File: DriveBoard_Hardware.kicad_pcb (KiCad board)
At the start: 2 copper layers, 124.5 x 121.7 mm, 48 parts, among them SW1 SW_DPDT_x2, U1 MAX_3232, U10 Left Back, U11 TM4C129E_Launchpad_Full, U12 IRF7821PbF, U13 IRF7821PbF, U14 IRF7821PbF, U15 Strip_1, U16 Strip_2, U17 Servo_1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

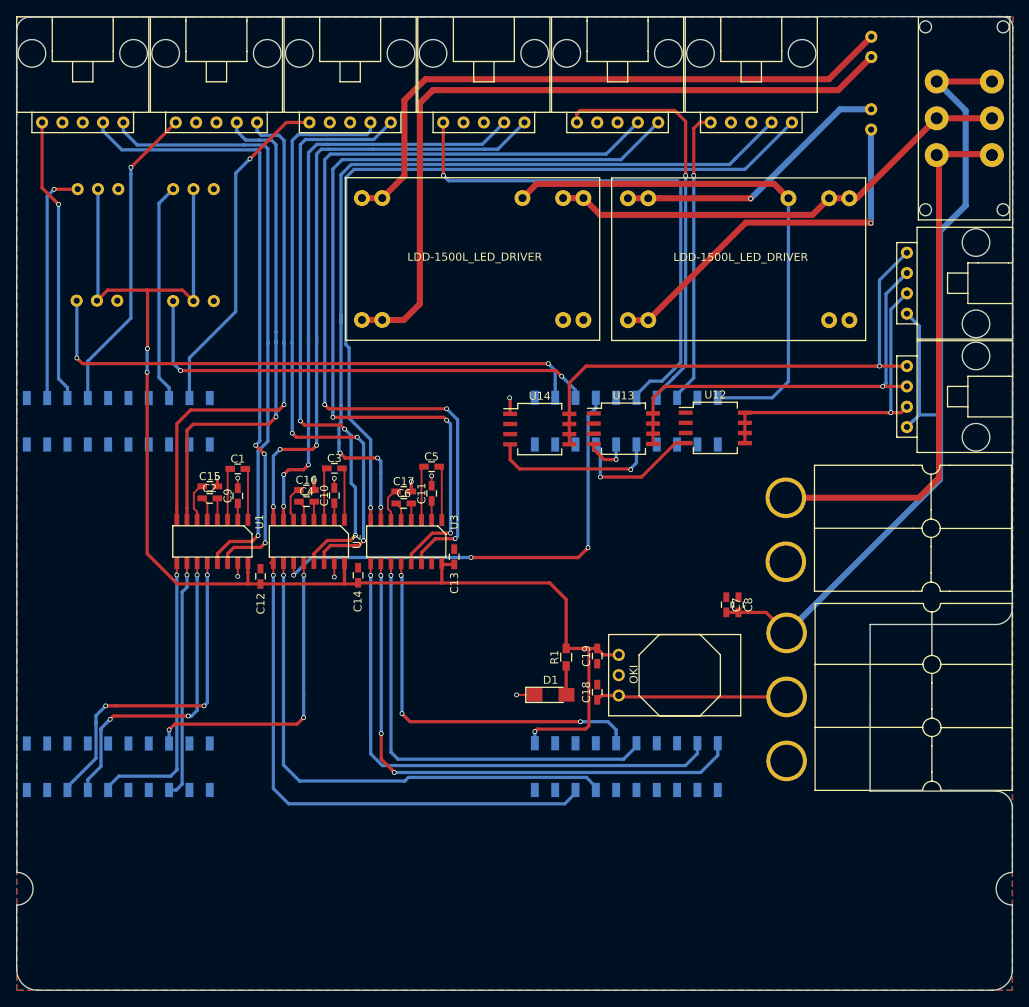
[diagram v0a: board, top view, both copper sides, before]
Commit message: Edited Schematic and added silkscreen
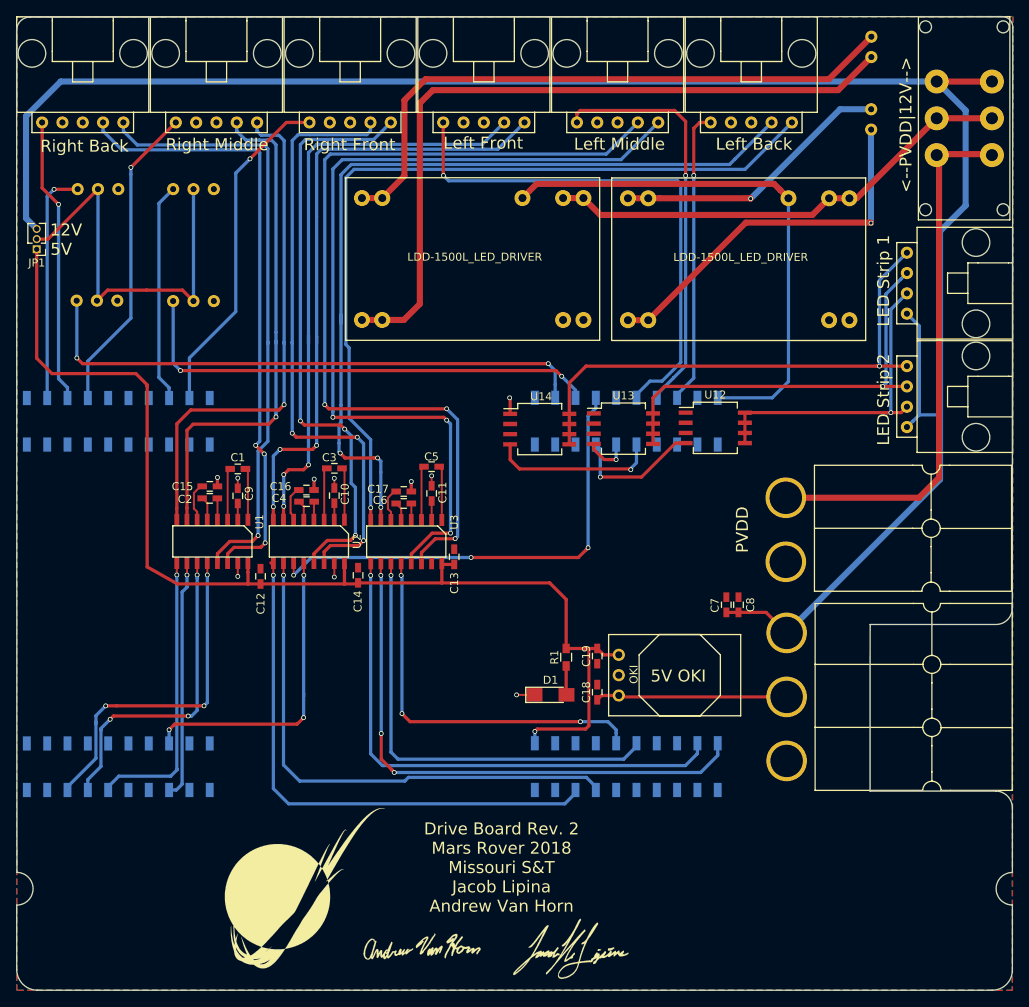
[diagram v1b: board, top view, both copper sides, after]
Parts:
- added G***: LOGO, MRDT_Silkscreens:MRDT_Logo_20mm, F.Cu at (169.7, 142.7)
- added G***: LOGO, MRDT_Silkscreens:Jacob_Lipina_Sig_15mm, F.Cu at (202.9, 150.5)
- added G***: LOGO, MRDT_Silkscreens:Andrew_Van_Horn_Sig_15mm, F.Cu at (184.3, 149.9)
- added JP1: Jumper_NC_Dual, Pin_Headers:Pin_Header_Straight_1x03_Pitch1.27mm, F.Cu at (136.2, 62.9)
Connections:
- U10 pad 2: (no net) -> Net-(U10-Pad2)
- U11 pad +5V: Net-(U11-Pad+5V) -> +5V
- U11 pad PB2: (no net) -> Net-(U11-PadPB2)
- U11 pad PB3: (no net) -> Net-(U11-PadPB3)
- U11 pad PD0: (no net) -> Net-(U11-PadPD0)
- U11 pad PD1: (no net) -> Net-(U11-PadPD1)
- U11 pad PD3: (no net) -> Net-(U11-PadPD3)
- U11 pad PD7: (no net) -> Net-(U11-PadPD7)
- U11 pad PE0: (no net) -> Net-(U11-PadPE0)
- U11 pad PE1: (no net) -> Net-(U11-PadPE1)
- U11 pad PE2: (no net) -> Net-(U11-PadPE2)
- U11 pad PE3: (no net) -> Net-(U11-PadPE3)
- U11 pad PE4: (no net) -> Net-(U11-PadPE4)
- U11 pad PE5: (no net) -> Net-(U11-PadPE5)
- U11 pad PF1: (no net) -> Net-(U11-PadPF1)
- U11 pad PF2: (no net) -> Net-(U11-PadPF2)
- U11 pad PF3: (no net) -> Net-(U11-PadPF3)
- U11 pad PG0: (no net) -> Net-(U11-PadPG0)
- U11 pad PG1: (no net) -> Net-(U11-PadPG1)
- U11 pad PH0: (no net) -> Net-(U11-PadPH0)
- U11 pad PH1: (no net) -> Net-(U11-PadPH1)
- U11 pad PK4: (no net) -> Net-(U11-PadPK4)
- U11 pad PK5: (no net) -> Net-(U11-PadPK5)
- U11 pad PK6: (no net) -> Net-(U11-PadPK6)
- U11 pad PK7: (no net) -> Net-(U11-PadPK7)
- U11 pad PL0: (no net) -> Net-(U11-PadPL0)
- U11 pad PL1: (no net) -> Net-(U11-PadPL1)
- U11 pad PL2: (no net) -> Net-(U11-PadPL2)
- U11 pad PL3: (no net) -> Net-(U11-PadPL3)
- U11 pad PL4: (no net) -> Net-(U11-PadPL4)
- U11 pad PL5: (no net) -> Net-(U11-PadPL5)
- U11 pad PM4: (no net) -> Net-(U11-PadPM4)
- U11 pad PM5: (no net) -> Net-(U11-PadPM5)
- U11 pad PP2: (no net) -> Net-(U11-PadPP2)
- U11 pad PQ1: (no net) -> Net-(U11-PadPQ1)
- U17 pad 2: +5V -> Net-(JP1-Pad2)
- U18 pad 2: +5V -> Net-(JP1-Pad2)
- U19 pad 2: +5V -> Net-(JP1-Pad2)
- U20 pad 2: +5V -> Net-(JP1-Pad2)
- U5 pad 2: (no net) -> Net-(U5-Pad2)
- U6 pad 2: (no net) -> Net-(U6-Pad2)
- U7 pad 2: (no net) -> Net-(U7-Pad2)
- U8 pad 2: (no net) -> Net-(U8-Pad2)
- U9 pad 2: (no net) -> Net-(U9-Pad2)
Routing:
- net +12V: track 113.3 -> 243.6 mm
- net Net-(JP1-Pad2): track 0.00 -> 51.4 mm
- net +5V: track 169.6 -> 146.1 mm, vias 3 -> 1
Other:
- board text added: "12V"
- board text added: "5V"
- board text added: "5V OKI"
- board text added: "<--PVDD|12V-->"
- board text added: "Drive Board Rev. 2 Mars Rover 2018 Missouri S&T Jacob Lipina Andrew Van Horn"
- board text added: "Headlight 1"
- board text added: "Headlight 2"
- board text added: "LED Strip 1"
- board text added: "LED Strip 2"
- board text added: "Left Back"
- board text added: "Left Front"
- board text added: "Left Middle"
- board text added: "PVDD"
- board text added: "Right Back"
- board text added: "Right Front"
- board text added: "Right Middle"
- board text added: "Servo 1"
- board text added: "Servo 2"
- board text added: "Servo 3"
- board text added: "Servo 4"
